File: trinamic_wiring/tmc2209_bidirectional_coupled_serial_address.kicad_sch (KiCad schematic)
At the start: 3 parts

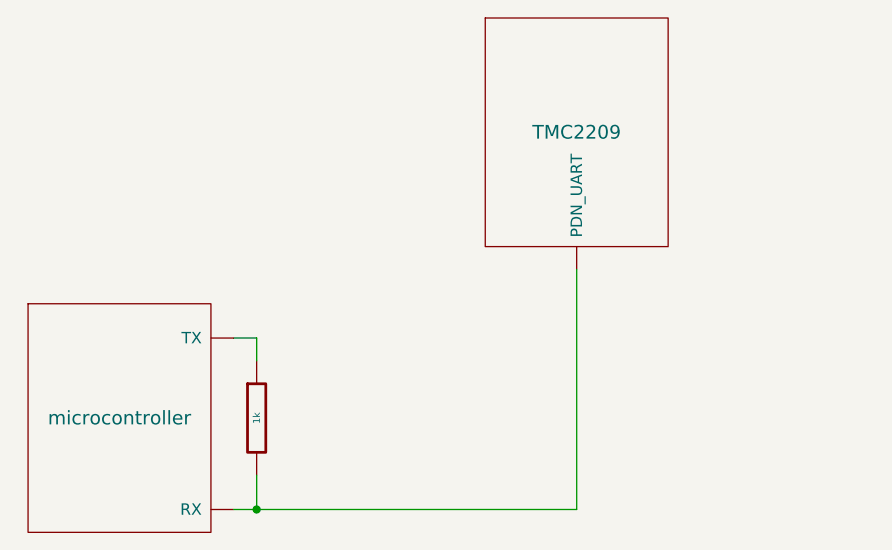
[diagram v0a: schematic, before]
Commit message: Add multiple chip schematics
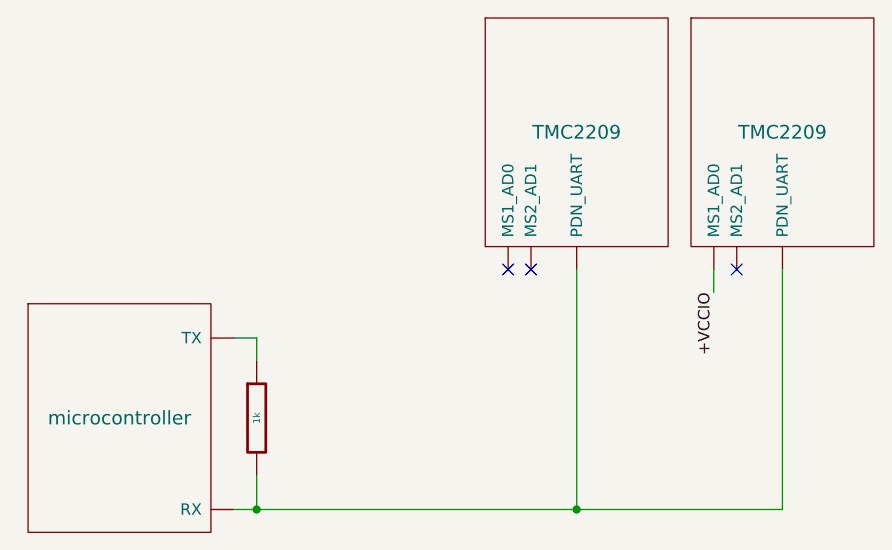
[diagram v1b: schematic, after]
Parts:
- removed TMC?: TMC2209, symbol Janelia:SIMPLIFIED_TMC2209_UART
- added TMC2, TMC3: TMC2209, symbol Janelia:SIMPLIFIED_TMC2209_ADDRESSES
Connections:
- net at R2.2, microcontroller?.0 (RX): now also TMC2.0 (PDN_UART), TMC3.0 (PDN_UART)
- new net +VCCIO: TMC3.2 (MS1_AD0)
- no-connect marks 0 -> 3
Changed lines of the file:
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@@
   (junction (at 102.87 106.68) (diameter 0) (color 0 0 0 0)
   )
+  (junction (at 138.43 106.68) (diameter 0) (color 0 0 0 0)
+  )
+  (no_connect (at 133.35 80.01))
+  (no_connect (at 130.81 80.01))
+  (no_connect (at 156.21 80.01))
   (wire (pts (xy 102.87 87.63) (xy 102.87 90.17))
+    (stroke (width 0) (type default))
+  )
+  (wire (pts (xy 161.29 80.01) (xy 161.29 106.68))
+    (stroke (width 0) (type default))
+  )
+  (wire (pts (xy 153.67 80.01) (xy 153.67 82.55))
+    (stroke (width 0) (type default))
+  )
+  (wire (pts (xy 138.43 106.68) (xy 161.29 106.68))
     (stroke (width 0) (type default))
   )
@@
   (wire (pts (xy 100.33 106.68) (xy 102.87 106.68))
     (stroke (width 0) (type default))
+  )
+  (label "+VCCIO" (at 153.67 82.55 270) (fields_autoplaced)
+    (effects (font (size 1.27 1.27)) (justify right bottom))
   )
   (symbol (lib_id "Janelia:SIMPLIFIED_MCU_UART") (at 87.63 96.52 0) (unit 1)
@@
     )
   )
-  (symbol (lib_id "Janelia:SIMPLIFIED_TMC2209_UART") (at 138.43 64.77 0) (unit 1)
-    (in_bom yes) (on_board yes) (dnp no) (fields_autoplaced)
-    (property "Reference" "TMC?" (at 138.43 64.77 0) (do_not_autoplace)
+  (symbol (lib_id "Janelia:SIMPLIFIED_TMC2209_ADDRESSES") (at 138.43 64.77 0) (unit 1)
+    (in_bom yes) (on_board yes) (dnp no)
+    (property "Reference" "TMC2" (at 138.43 64.77 0) (do_not_autoplace)
       (effects (font (size 1.524 1.524)) hide)
     )
-    (property "Value" "TMC2209" (at 138.43 64.77 0)
+    (property "Value" "TMC2209" (at 138.43 64.77 0) (do_not_autoplace)
       (effects (font (size 1.524 1.524)))
     )
@@
     )
     (pin "0")
+    (pin "1")
+    (pin "2")
     (instances
       (project "trinamic_wiring"
-        (path "/e4144788-6304-493f-818e-5d881d3b7418/c8eda2b5-ab13-4033-82d9-875c9fcaf884/13e2a7b5-46df-44bb-8dde-5d79d190b8bf"
-          (reference "TMC?") (unit 1)
-        )
-        (path "/e4144788-6304-493f-818e-5d881d3b7418/c8eda2b5-ab13-4033-82d9-875c9fcaf884/e3613d8e-f506-47d6-ad2d-b0f5798d9847"
-          (reference "TMC1") (unit 1)
-        )
         (path "/e4144788-6304-493f-818e-5d881d3b7418/c8eda2b5-ab13-4033-82d9-875c9fcaf884/5f6f310d-167d-42a3-8815-1b623fe73dc8"
           (reference "TMC2") (unit 1)
@@
         )
       )
+    )
+  )
+  (symbol (lib_id "Janelia:SIMPLIFIED_TMC2209_ADDRESSES") (at 161.29 64.77 0) (unit 1)
+    (in_bom yes) (on_board yes) (dnp no)
+    (property "Reference" "TMC3" (at 161.29 64.77 0) (do_not_autoplace)
+      (effects (font (size 1.524 1.524)) hide)
+    )
+    (property "Value" "TMC2209" (at 161.29 64.77 0) (do_not_autoplace)
+      (effects (font (size 1.524 1.524)))
+    )
+    (property "Footprint" "" (at 158.75 91.44 0)
+      (effects (font (size 1.524 1.524)) hide)
+    )
+    (property "Datasheet" "" (at 161.29 64.77 0)
+      (effects (font (size 1.524 1.524)) hide)
+    )
+    (pin "0")
+    (pin "1")
+    (pin "2")
+    (instances
+      (project "trinamic_wiring"
+        (path "/e4144788-6304-493f-818e-5d881d3b7418/c8eda2b5-ab13-4033-82d9-875c9fcaf884/5f6f310d-167d-42a3-8815-1b623fe73dc8"
+          (reference "TMC3") (unit 1)
+        )
+      )
